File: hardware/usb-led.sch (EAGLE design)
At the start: 12 parts, among them U1 Tiny85-20-SMT

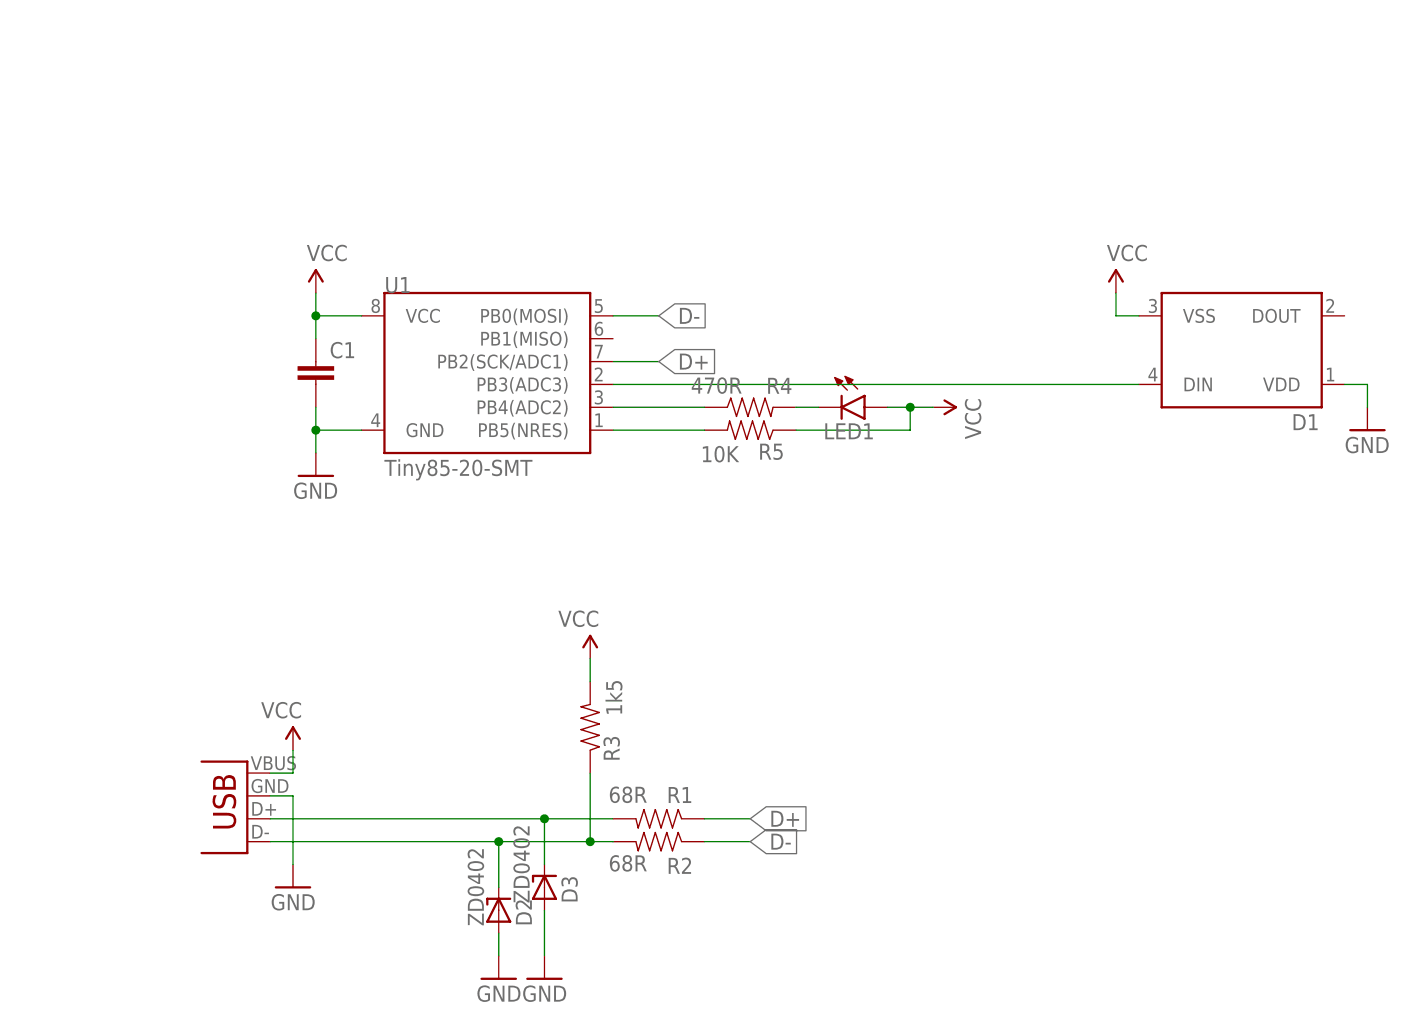
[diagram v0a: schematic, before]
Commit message: Hardware: revision 2
- Fix: WS2812Bs DIN/DOUT pins were swapped. This was a bug in
  SparkFuns eagle library (fixed in latest version).

- Smaller board: border now cuts through USB plug mounting via.
  OSHPark support said it's fine. We'll see.
  If it doesn't work, I'll have to either use the larger board size,
  find an (expensive) SMD male USB A connector or use a PCB connector
  (and switch to a fab that supports 2.4mm thick boards).

- No 0402 components (R, ZD) anymore. The smallest are 0603 now.
  I can solder 0402, but it's not very beginner-friendly.

- Add 0805 10uF bulk capacitance, just in case. It seems to work fine
  without, so it doesn't need to be populated. (Cost: 18ct at Qty 1)

- Move components that were in the way of my uC test clip.
  I've also added a bKeepout polygon.

- Values for remaining parts (e.g. zener diodes: 3.6V)

- Increase text size from 16mil to 24mil.
  The 16mil texts didn't turn out well.

- Cosmetics.
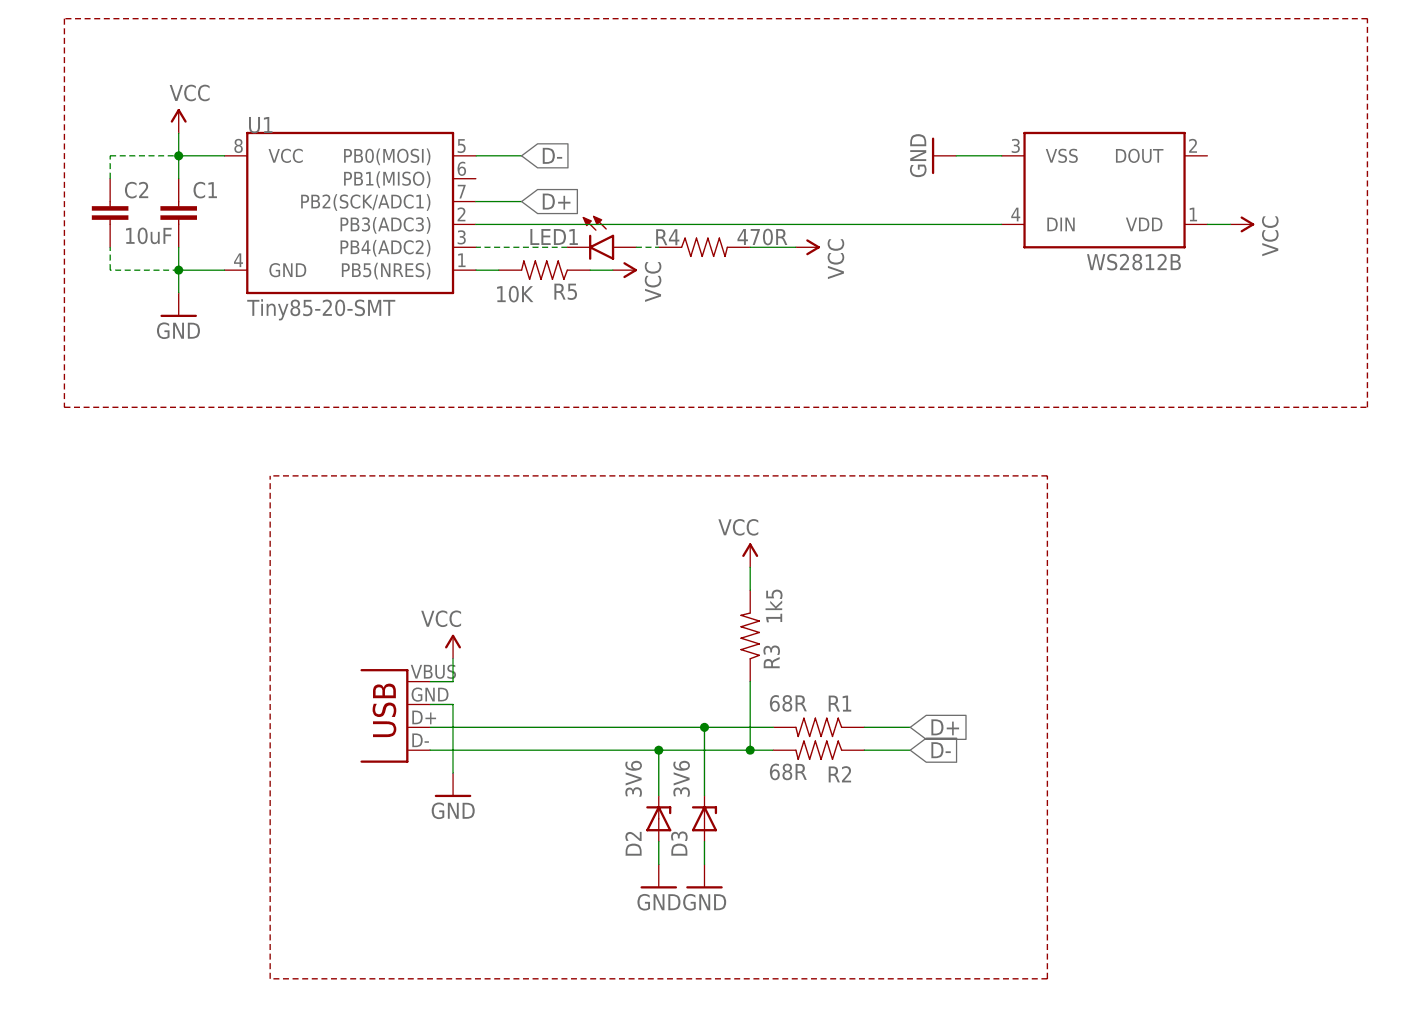
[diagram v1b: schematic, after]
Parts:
- removed D1: (no value), SparkFun-LED:WS2812B
- added C2: 10uF, rcl:C-EUC0805
- added WS2812B: (no value), SparkFun-LED:WS2812B
- D2, D3: value ZD0402 -> 3V6; device z-diode-0402:ZD0402 -> z-diode-0603:ZD0603
- R1, R2, R3: device SparkFun-Passives:RESISTOR0402-RES -> SparkFun-Resistors:RESISTOR0603
- R5: device SparkFun-Passives:RESISTOR0402-RES -> SparkFun-Resistors:RESISTOR0603-RES
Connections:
- removed net N$7: D1.DIN, U1.PB3(ADC3)
- new net DIN: U1.PB3(ADC3), WS2812B.DIN
- net GND: now also C2.2, WS2812B.VSS; no longer D1.VDD
- net N$3: now also LED1.C; no longer R4.1
- net N$4: now also LED1.A, R4.1; no longer LED1.C, R4.2
- net VCC: now also C2.1, R4.2, WS2812B.VDD; no longer D1.VSS, LED1.A
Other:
- moved on the sheet: C1, D2, D3, LED1, R1, R2, R3, R4, R5, U1

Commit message: Hardware: rename parts
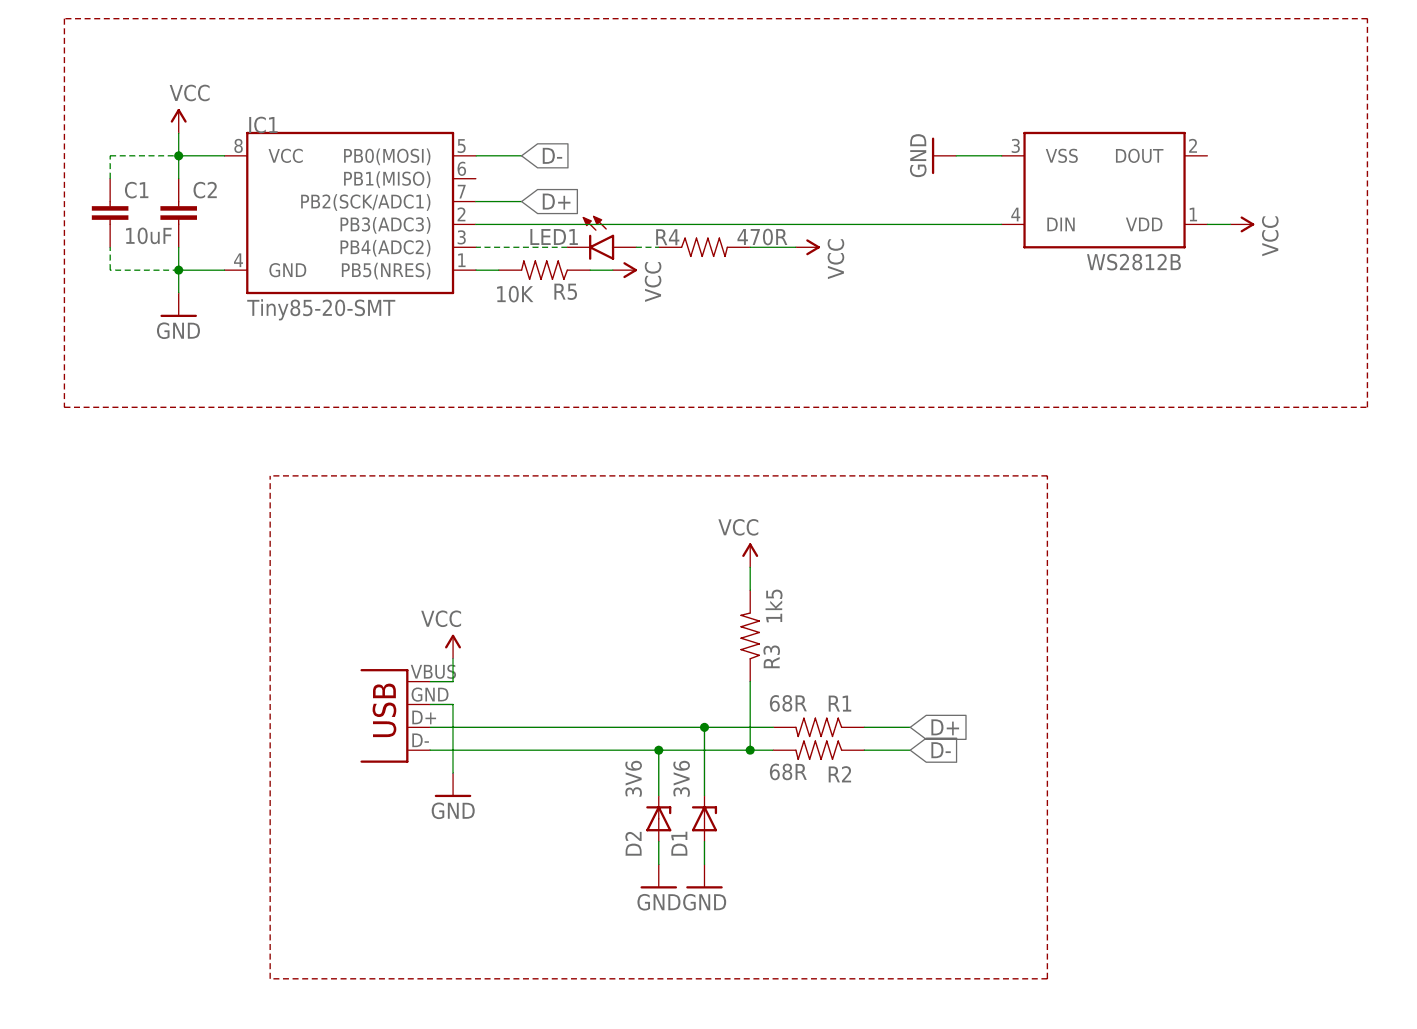
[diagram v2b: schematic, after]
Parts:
- C1: value (none) -> 10uF; device SparkFun-Passives:CAP0805 -> rcl:C-EUC0805
- C2: value 10uF -> (none); device rcl:C-EUC0805 -> SparkFun-Passives:CAP0805
- renumbered D3 to D1, JP2 to USB, U1 to IC1
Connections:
- net N$1 renamed EXT_D+
- net N$2 renamed EXT_D-
- net N$5 renamed C10
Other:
- moved on the sheet: C1, C2

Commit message: Hardware: more space for the Zener diodes
Their case is a a little bit larger than the normal 0603 footprint.
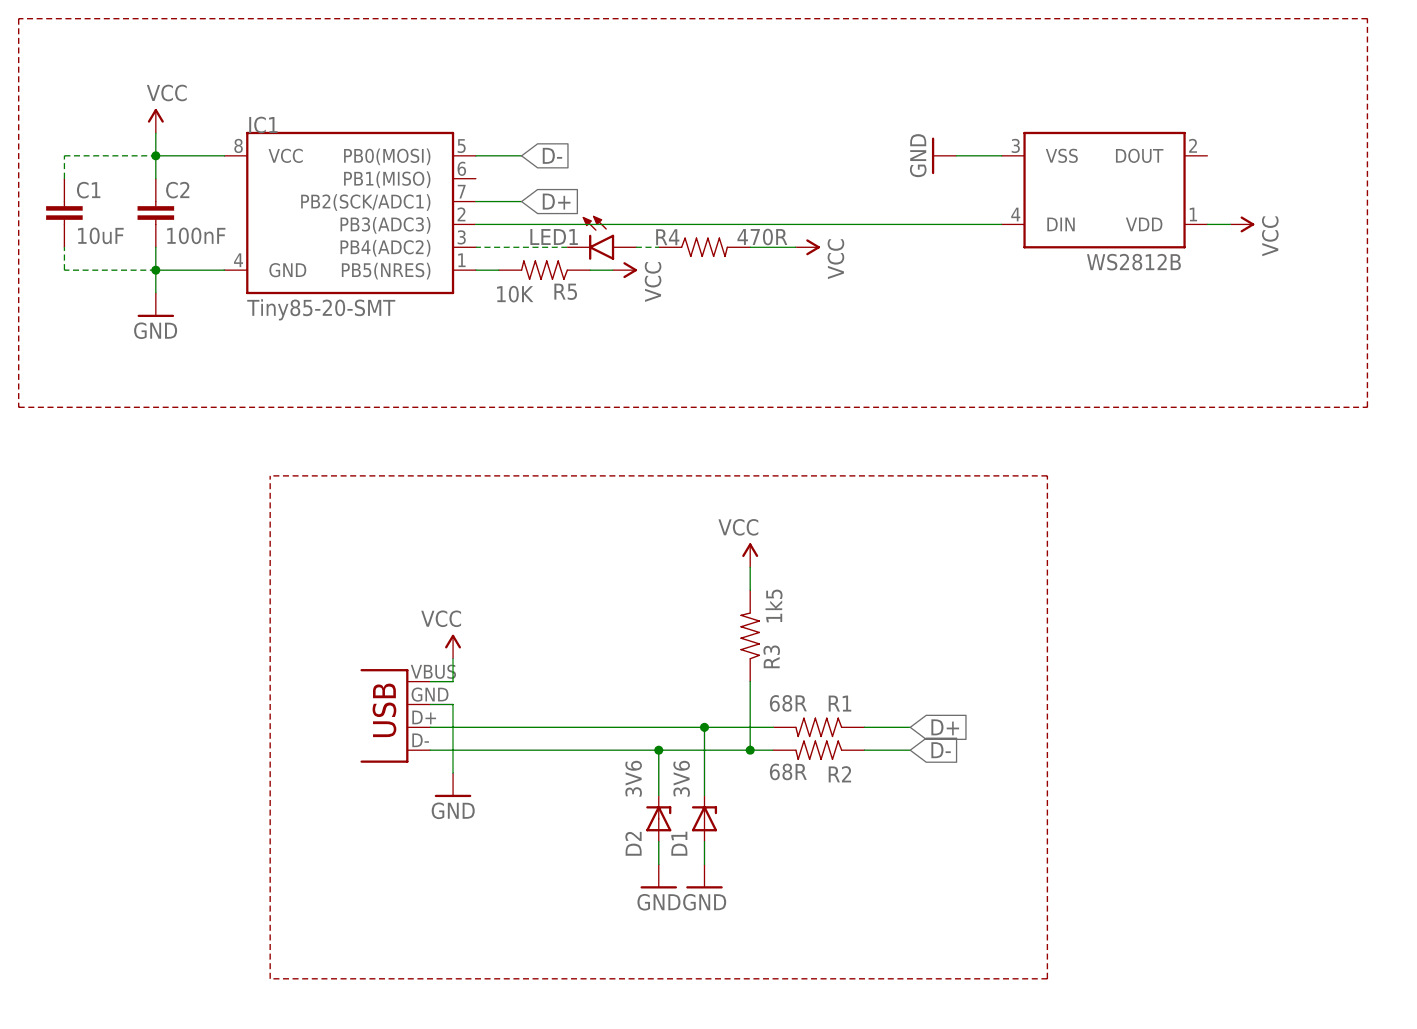
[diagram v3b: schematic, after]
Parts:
- C2: value (none) -> 100nF
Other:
- moved on the sheet: C1, C2
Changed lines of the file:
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@@
 <part name="GND2" library="SparkFun-Aesthetics" deviceset="GND" device=""/>
 <part name="SUPPLY4" library="SparkFun-Aesthetics" deviceset="VCC" device=""/>
-<part name="C2" library="SparkFun-Passives" deviceset="CAP" device="0805"/>
+<part name="C2" library="SparkFun-Passives" deviceset="CAP" device="0805" value="100nF"/>
 <part name="GND3" library="SparkFun-Aesthetics" deviceset="GND" device=""/>
 <part name="SUPPLY3" library="SparkFun-Aesthetics" deviceset="VCC" device=""/>
@@
 <wire x1="175.26" y1="45.72" x2="175.26" y2="101.6" width="0.1524" layer="94" style="longdash"/>
 <wire x1="175.26" y1="101.6" x2="88.9" y2="101.6" width="0.1524" layer="94" style="longdash"/>
-<wire x1="66.04" y1="152.4" x2="66.04" y2="109.22" width="0.1524" layer="94" style="longdash"/>
-<wire x1="66.04" y1="109.22" x2="210.82" y2="109.22" width="0.1524" layer="94" style="longdash"/>
+<wire x1="60.96" y1="152.4" x2="60.96" y2="109.22" width="0.1524" layer="94" style="longdash"/>
+<wire x1="60.96" y1="109.22" x2="210.82" y2="109.22" width="0.1524" layer="94" style="longdash"/>
 <wire x1="210.82" y1="109.22" x2="210.82" y2="152.4" width="0.1524" layer="94" style="longdash"/>
-<wire x1="210.82" y1="152.4" x2="66.04" y2="152.4" width="0.1524" layer="94" style="longdash"/>
+<wire x1="210.82" y1="152.4" x2="60.96" y2="152.4" width="0.1524" layer="94" style="longdash"/>
 </plain>
 <instances>
@@
 <attribute name="VALUE" x="144.018" y="85.09" size="1.778" layer="96" rot="MR90"/>
 </instance>
-<instance part="SUPPLY2" gate="G$1" x="78.74" y="139.7"/>
-<instance part="GND2" gate="1" x="78.74" y="119.38"/>
+<instance part="SUPPLY2" gate="G$1" x="76.2" y="139.7"/>
+<instance part="GND2" gate="1" x="76.2" y="119.38"/>
 <instance part="SUPPLY4" gate="G$1" x="142.24" y="91.44" rot="MR0"/>
-<instance part="C2" gate="G$1" x="78.74" y="129.54"/>
+<instance part="C2" gate="G$1" x="76.2" y="129.54" smashed="yes">
+<attribute name="NAME" x="77.216" y="132.461" size="1.778" layer="95"/>
+<attribute name="VALUE" x="77.216" y="127.381" size="1.778" layer="96"/>
+</instance>
 <instance part="GND3" gate="1" x="162.56" y="137.16" rot="R270"/>
 <instance part="SUPPLY3" gate="G$1" x="195.58" y="129.54" rot="R270"/>
@@
 <attribute name="VALUE" x="135.509" y="65.786" size="1.778" layer="96" rot="R90"/>
 </instance>
-<instance part="C1" gate="G$1" x="71.12" y="132.08"/>
+<instance part="C1" gate="G$1" x="66.04" y="132.08" smashed="yes">
+<attribute name="NAME" x="67.31" y="132.461" size="1.778" layer="95"/>
+<attribute name="VALUE" x="67.31" y="127.381" size="1.778" layer="96"/>
+</instance>
 <instance part="SUPPLY1" gate="G$1" x="127" y="124.46" rot="R270"/>
 </instances>
@@
 <segment>
 <pinref part="IC1" gate="G$1" pin="GND"/>
-<wire x1="83.82" y1="124.46" x2="78.74" y2="124.46" width="0.1524" layer="91"/>
-<wire x1="78.74" y1="124.46" x2="78.74" y2="121.92" width="0.1524" layer="91"/>
+<wire x1="83.82" y1="124.46" x2="76.2" y2="124.46" width="0.1524" layer="91"/>
+<wire x1="76.2" y1="124.46" x2="76.2" y2="121.92" width="0.1524" layer="91"/>
 <pinref part="GND2" gate="1" pin="GND"/>
 <pinref part="C2" gate="G$1" pin="2"/>
-<wire x1="78.74" y1="124.46" x2="78.74" y2="127" width="0.1524" layer="91"/>
-<junction x="78.74" y="124.46"/>
+<wire x1="76.2" y1="124.46" x2="76.2" y2="127" width="0.1524" layer="91"/>
+<junction x="76.2" y="124.46"/>
 <pinref part="C1" gate="G$1" pin="2"/>
-<wire x1="78.74" y1="124.46" x2="71.12" y2="124.46" width="0.1524" layer="91" style="longdash"/>
-<wire x1="71.12" y1="124.46" x2="71.12" y2="127" width="0.1524" layer="91" style="longdash"/>
+<wire x1="76.2" y1="124.46" x2="66.04" y2="124.46" width="0.1524" layer="91" style="longdash"/>
+<wire x1="66.04" y1="124.46" x2="66.04" y2="127" width="0.1524" layer="91" style="longdash"/>
 </segment>
 <segment>
@@
 <segment>
 <pinref part="IC1" gate="G$1" pin="VCC"/>
-<wire x1="83.82" y1="137.16" x2="78.74" y2="137.16" width="0.1524" layer="91"/>
-<wire x1="78.74" y1="137.16" x2="78.74" y2="139.7" width="0.1524" layer="91"/>
+<wire x1="83.82" y1="137.16" x2="76.2" y2="137.16" width="0.1524" layer="91"/>
+<wire x1="76.2" y1="137.16" x2="76.2" y2="139.7" width="0.1524" layer="91"/>
 <pinref part="SUPPLY2" gate="G$1" pin="VCC"/>
 <pinref part="C2" gate="G$1" pin="1"/>
-<wire x1="78.74" y1="134.62" x2="78.74" y2="137.16" width="0.1524" layer="91"/>
-<junction x="78.74" y="137.16"/>
+<wire x1="76.2" y1="134.62" x2="76.2" y2="137.16" width="0.1524" layer="91"/>
+<junction x="76.2" y="137.16"/>
 <pinref part="C1" gate="G$1" pin="1"/>
-<wire x1="71.12" y1="134.62" x2="71.12" y2="137.16" width="0.1524" layer="91" style="longdash"/>
-<wire x1="71.12" y1="137.16" x2="78.74" y2="137.16" width="0.1524" layer="91" style="longdash"/>
+<wire x1="66.04" y1="134.62" x2="66.04" y2="137.16" width="0.1524" layer="91" style="longdash"/>
+<wire x1="66.04" y1="137.16" x2="76.2" y2="137.16" width="0.1524" layer="91" style="longdash"/>
 </segment>
 <segment>
